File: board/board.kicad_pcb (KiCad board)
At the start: 2 copper layers, 96.8 x 80.9 mm, 32 parts, among them J1 RPi_Header, J2 Smoke_Sensor, J3 LEDs, J4 Temp_Sensor, J5 Alarm, J6 Conn_01x03, J7 Fan_Power, J8 USB_Power, J9 Coil, Q1 Q_PMOS_GDS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

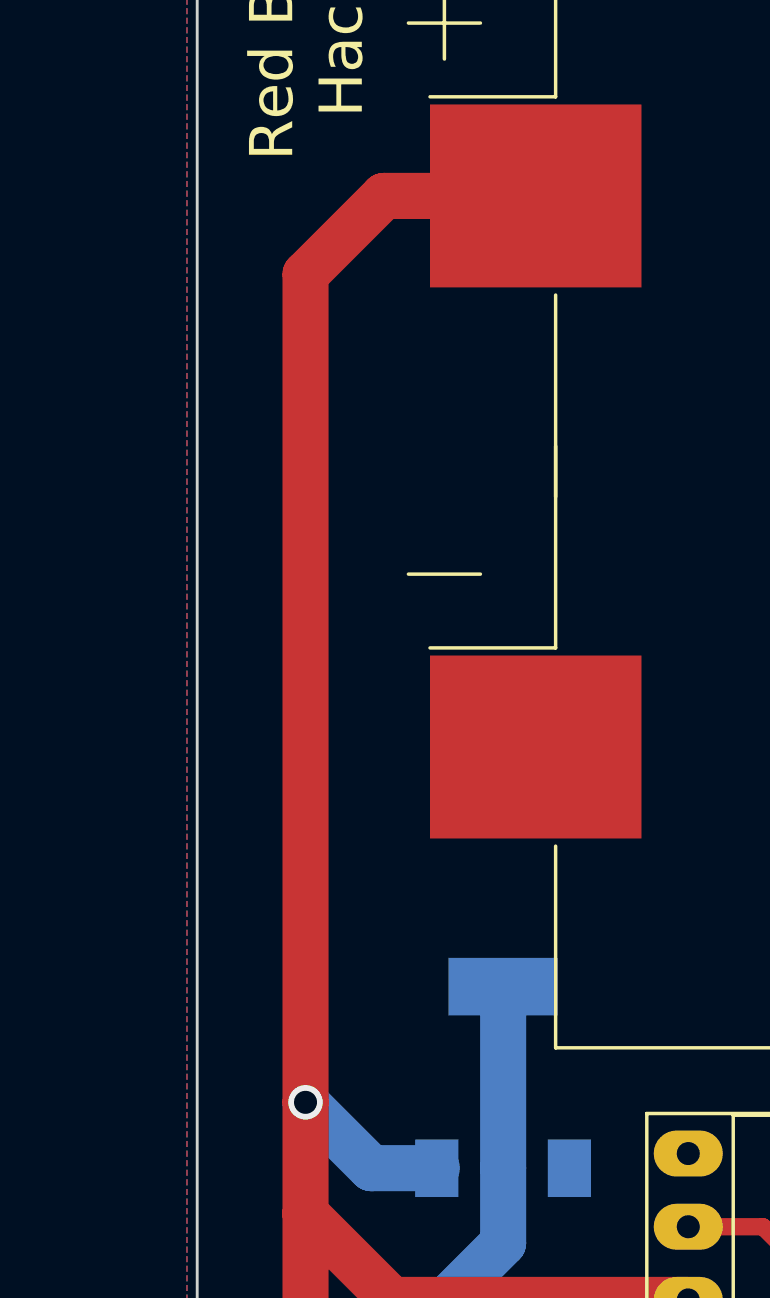
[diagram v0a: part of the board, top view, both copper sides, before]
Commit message: Fixed and panelized
Added text to RS232 board
Added on/off switch to main board
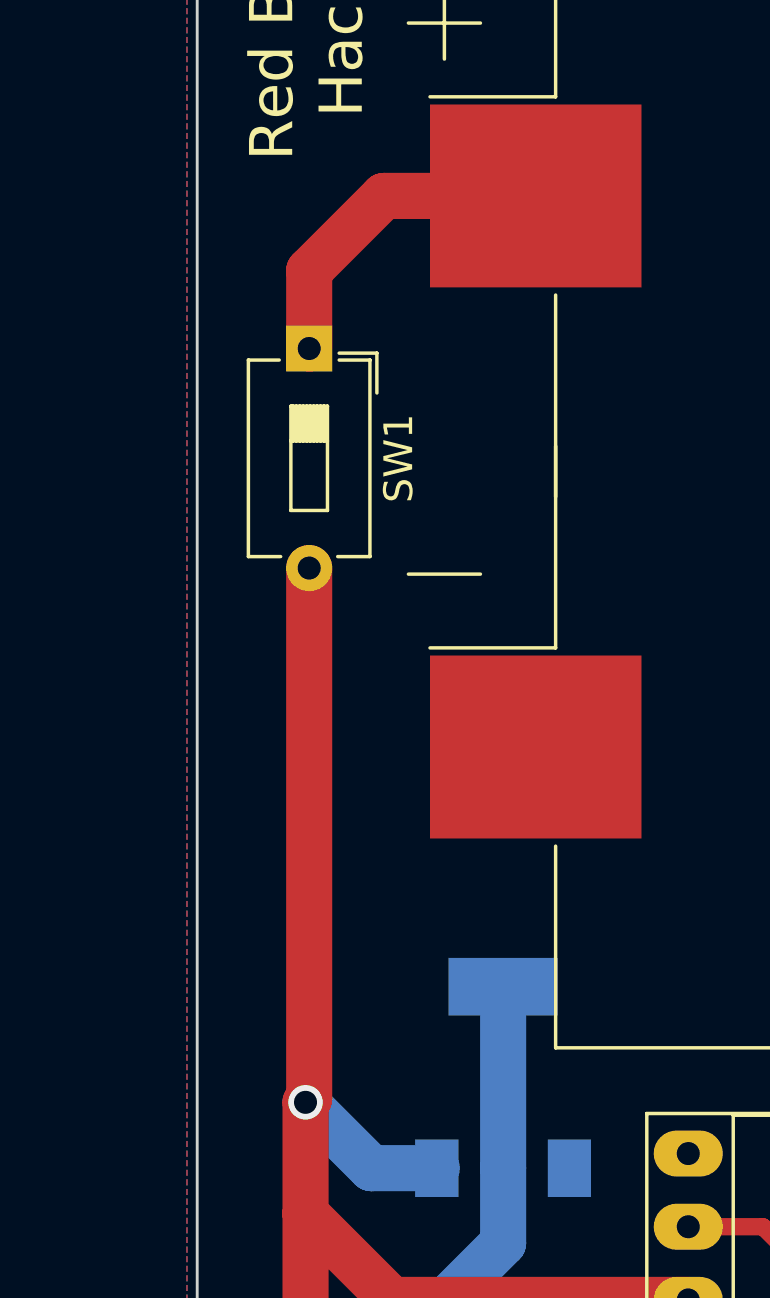
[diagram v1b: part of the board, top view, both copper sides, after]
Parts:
- added SW1: SW_DIP_x01, Button_Switch_THT:SW_DIP_SPSTx01_Slide_6.7x4.1mm_W7.62mm_P2.54mm_LowProfile, F.Cu at (70.4, 95.6)
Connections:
- BT1 pad 1: +7.5V -> Net-(BT1-Pad1)
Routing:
- net +7.5V: track 214.5 -> 195.2 mm
- net Net-(BT1-Pad1): track 0.00 -> 11.6 mm
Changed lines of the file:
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@@
     (thickness 1.6)
     (drawings 23)
-    (tracks 165)
+    (tracks 167)
     (zones 0)
-    (modules 32)
-    (nets 55)
+    (modules 33)
+    (nets 56)
   )
   (page A4)
@@
   (net 53 "Net-(U2-Pad8)")
   (net 54 "Net-(BT1-Pad2)")
+  (net 55 "Net-(BT1-Pad1)")
   (net_class Default "This is the default net class."
     (clearance 0.4)
@@
     (add_net /UART_TX_WHT)
     (add_net GND)
+    (add_net "Net-(BT1-Pad1)")
     (add_net "Net-(BT1-Pad2)")
     (add_net "Net-(C5-Pad1)")
@@
     (pad "" np_thru_hole circle (at -27.6 17.5631) (size 3.45 3.45) (drill 3.45) (layers *.Cu *.Mask))
     (pad 1 smd rect (at -39.33 -9.5631) (size 7.34 6.35) (layers F.Cu F.Paste F.Mask)
-      (net 2 +7.5V))
+      (net 55 "Net-(BT1-Pad1)"))
     (pad 2 smd rect (at 39.33 -9.5631) (size 7.34 6.35) (layers F.Cu F.Paste F.Mask)
       (net 54 "Net-(BT1-Pad2)"))
@@
       (xy 1.126492 -15.143947)) (layer B.SilkS) (width 0.01))
   )
+  (module Button_Switch_THT:SW_DIP_SPSTx01_Slide_6.7x4.1mm_W7.62mm_P2.54mm_LowProfile (layer F.Cu)
+    (at 70.4088 95.5548 270)
+    (descr "1x-dip-switch SPST , Slide, row spacing 7.62 mm (300 mils), body size 6.7x4.1mm (see e.g. https://www.ctscorp.com/wp-content/uploads/209-210.pdf), LowProfile")
+    (tags "DIP Switch SPST Slide 7.62mm 300mil LowProfile")
+    (fp_text reference SW1 (at 3.81 -3.11 270) (layer F.SilkS)
+      (effects (font (size 1 1) (thickness 0.15)))
+    )
+    (fp_text value SW_DIP_x01 (at 3.81 3.11 270) (layer F.Fab) hide
+      (effects (font (size 1 1) (thickness 0.15)))
+    )
+    (fp_line (start 1.46 -2.05) (end 7.16 -2.05) (layer F.Fab) (width 0.1))
+    (fp_line (start 7.16 -2.05) (end 7.16 2.05) (layer F.Fab) (width 0.1))
+    (fp_line (start 7.16 2.05) (end 0.46 2.05) (layer F.Fab) (width 0.1))
+    (fp_line (start 0.46 2.05) (end 0.46 -1.05) (layer F.Fab) (width 0.1))
+    (fp_line (start 0.46 -1.05) (end 1.46 -2.05) (layer F.Fab) (width 0.1))
+    (fp_line (start 2 -0.635) (end 2 0.635) (layer F.Fab) (width 0.1))
+    (fp_line (start 2 0.635) (end 5.62 0.635) (layer F.Fab) (width 0.1))
+    (fp_line (start 5.62 0.635) (end 5.62 -0.635) (layer F.Fab) (width 0.1))
+    (fp_line (start 5.62 -0.635) (end 2 -0.635) (layer F.Fab) (width 0.1))
+    (fp_line (start 2 -0.535) (end 3.206667 -0.535) (layer F.Fab) (width 0.1))
+    (fp_line (start 2 -0.435) (end 3.206667 -0.435) (layer F.Fab) (width 0.1))
+    (fp_line (start 2 -0.335) (end 3.206667 -0.335) (layer F.Fab) (width 0.1))
+    (fp_line (start 2 -0.235) (end 3.206667 -0.235) (layer F.Fab) (width 0.1))
+    (fp_line (start 2 -0.135) (end 3.206667 -0.135) (layer F.Fab) (width 0.1))
+    (fp_line (start 2 -0.035) (end 3.206667 -0.035) (layer F.Fab) (width 0.1))
+    (fp_line (start 2 0.065) (end 3.206667 0.065) (layer F.Fab) (width 0.1))
+    (fp_line (start 2 0.165) (end 3.206667 0.165) (layer F.Fab) (width 0.1))
+    (fp_line (start 2 0.265) (end 3.206667 0.265) (layer F.Fab) (width 0.1))
+    (fp_line (start 2 0.365) (end 3.206667 0.365) (layer F.Fab) (width 0.1))
+    (fp_line (start 2 0.465) (end 3.206667 0.465) (layer F.Fab) (width 0.1))
+    (fp_line (start 2 0.565) (end 3.206667 0.565) (layer F.Fab) (width 0.1))
+    (fp_line (start 3.206667 -0.635) (end 3.206667 0.635) (layer F.Fab) (width 0.1))
+    (fp_line (start 0.4 -2.11) (end 7.221 -2.11) (layer F.SilkS) (width 0.12))
+    (fp_line (start 0.4 2.11) (end 7.221 2.11) (layer F.SilkS) (width 0.12))
+    (fp_line (start 0.4 -2.11) (end 0.4 -1.04) (layer F.SilkS) (width 0.12))
+    (fp_line (start 0.4 1.04) (end 0.4 2.11) (layer F.SilkS) (width 0.12))
+    (fp_line (start 7.221 -2.11) (end 7.221 -0.99) (layer F.SilkS) (width 0.12))
+    (fp_line (start 7.221 0.99) (end 7.221 2.11) (layer F.SilkS) (width 0.12))
+    (fp_line (start 0.16 -2.35) (end 1.543 -2.35) (layer F.SilkS) (width 0.12))
+    (fp_line (start 0.16 -2.35) (end 0.16 -1.04) (layer F.SilkS) (width 0.12))
+    (fp_line (start 2 -0.635) (end 2 0.635) (layer F.SilkS) (width 0.12))
+    (fp_line (start 2 0.635) (end 5.62 0.635) (layer F.SilkS) (width 0.12))
+    (fp_line (start 5.62 0.635) (end 5.62 -0.635) (layer F.SilkS) (width 0.12))
+    (fp_line (start 5.62 -0.635) (end 2 -0.635) (layer F.SilkS) (width 0.12))
+    (fp_line (start 2 -0.515) (end 3.206667 -0.515) (layer F.SilkS) (width 0.12))
+    (fp_line (start 2 -0.395) (end 3.206667 -0.395) (layer F.SilkS) (width 0.12))
+    (fp_line (start 2 -0.275) (end 3.206667 -0.275) (layer F.SilkS) (width 0.12))
+    (fp_line (start 2 -0.155) (end 3.206667 -0.155) (layer F.SilkS) (width 0.12))
+    (fp_line (start 2 -0.035) (end 3.206667 -0.035) (layer F.SilkS) (width 0.12))
+    (fp_line (start 2 0.085) (end 3.206667 0.085) (layer F.SilkS) (width 0.12))
+    (fp_line (start 2 0.205) (end 3.206667 0.205) (layer F.SilkS) (width 0.12))
+    (fp_line (start 2 0.325) (end 3.206667 0.325) (layer F.SilkS) (width 0.12))
+    (fp_line (start 2 0.445) (end 3.206667 0.445) (layer F.SilkS) (width 0.12))
+    (fp_line (start 2 0.565) (end 3.206667 0.565) (layer F.SilkS) (width 0.12))
+    (fp_line (start 3.206667 -0.635) (end 3.206667 0.635) (layer F.SilkS) (width 0.12))
+    (fp_line (start -1.1 -2.4) (end -1.1 2.4) (layer F.CrtYd) (width 0.05))
+    (fp_line (start -1.1 2.4) (end 8.7 2.4) (layer F.CrtYd) (width 0.05))
+    (fp_line (start 8.7 2.4) (end 8.7 -2.4) (layer F.CrtYd) (width 0.05))
+    (fp_line (start 8.7 -2.4) (end -1.1 -2.4) (layer F.CrtYd) (width 0.05))
+    (fp_text user %R (at 6.39 0) (layer F.Fab)
+      (effects (font (size 0.6 0.6) (thickness 0.09)))
+    )
+    (fp_text user on (at 4.485 -1.3425 270) (layer F.Fab)
+      (effects (font (size 0.6 0.6) (thickness 0.09)))
+    )
+    (pad 1 thru_hole rect (at 0 0 270) (size 1.6 1.6) (drill 0.8) (layers *.Cu *.Mask)
+      (net 55 "Net-(BT1-Pad1)"))
+    (pad 2 thru_hole oval (at 7.62 0 270) (size 1.6 1.6) (drill 0.8) (layers *.Cu *.Mask)
+      (net 2 +7.5V))
+    (model ${KISYS3DMOD}/Button_Switch_THT.3dshapes/SW_DIP_SPSTx01_Slide_6.7x4.1mm_W7.62mm_P2.54mm_LowProfile.wrl
+      (at (xyz 0 0 0))
+      (scale (xyz 1 1 1))
+      (rotate (xyz 0 0 90))
+    )
+  )
   (gr_arc (start 68.7324 66.6242) (end 66.5226 66.6242) (angle 90) (layer Edge.Cuts) (width 0.1))
   (gr_arc (start 68.7324 143.1036) (end 68.7324 145.3134) (angle 90) (layer Edge.Cuts) (width 0.1))
@@
   (segment (start 158.3108 125.204) (end 158.3182 125.1966) (width 0.6) (layer B.Cu) (net 1))
   (segment (start 155.3464 125.204) (end 158.3108 125.204) (width 0.6) (layer B.Cu) (net 1))
-  (segment (start 73.002 90.2589) (end 70.2818 92.9791) (width 1.6) (layer F.Cu) (net 2))
-  (segment (start 78.272 90.2589) (end 73.002 90.2589) (width 1.6) (layer F.Cu) (net 2))
   (segment (start 101.7122 142.6718) (end 100.9142 142.6718) (width 1.6) (layer F.Cu) (net 2))
   (segment (start 103.2196 141.1644) (end 101.7122 142.6718) (width 1.6) (layer F.Cu) (net 2))
@@
   (via (at 70.2818 121.7168) (size 1.2) (drill 0.8) (layers F.Cu B.Cu) (net 2))
   (segment (start 72.5682 124.0032) (end 70.2818 121.7168) (width 1.6) (layer B.Cu) (net 2))
-  (segment (start 70.2818 92.9791) (end 70.2818 121.7168) (width 1.6) (layer F.Cu) (net 2))
   (segment (start 74.8398 124.0032) (end 72.5682 124.0032) (width 1.6) (layer B.Cu) (net 2))
   (segment (start 70.2818 121.7168) (end 70.2818 125.5776) (width 1.6) (layer F.Cu) (net 2))
@@
   (segment (start 119.3038 143.002) (end 118.9736 142.6718) (width 1.6) (layer F.Cu) (net 2))
   (segment (start 135.2804 143.002) (end 119.3038 143.002) (width 1.6) (layer F.Cu) (net 2))
+  (segment (start 70.4088 121.5898) (end 70.2818 121.7168) (width 1.6) (layer F.Cu) (net 2))
+  (segment (start 70.4088 103.1748) (end 70.4088 121.5898) (width 1.6) (layer F.Cu) (net 2))
   (segment (start 125.2396 140.419) (end 125.222 140.4366) (width 1.6) (layer F.Cu) (net 3))
   (segment (start 126.853401 139.586601) (end 125.2396 137.9728) (width 1.6) (layer F.Cu) (net 3))
@@
   (segment (start 156.932 95.0339) (end 156.932 109.3851) (width 1.6) (layer F.Cu) (net 54))
   (segment (start 156.932 90.2589) (end 156.932 95.0339) (width 1.6) (layer F.Cu) (net 54))
+  (segment (start 70.4088 92.8521) (end 70.4088 95.5548) (width 1.6) (layer F.Cu) (net 55))
+  (segment (start 78.272 90.2589) (end 73.002 90.2589) (width 1.6) (layer F.Cu) (net 55))
+  (segment (start 73.002 90.2589) (end 70.4088 92.8521) (width 1.6) (layer F.Cu) (net 55))
   (zone (net 1) (net_name GND) (layer F.Cu) (hatch edge 0.508)
     (connect_pads (clearance 0.508))
